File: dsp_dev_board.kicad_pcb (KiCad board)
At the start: 4 copper layers, 100 x 72.6 mm, 92 parts, among them J1 aux_mcu_power, J10 DX07S016JA1R1500, J11 Conn_02x11_Odd_Even, J2 audio_in, J3 audio_out, J4 9v_jack, J5 input_jack, J6 output_jack, J7 digital, J8 analog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

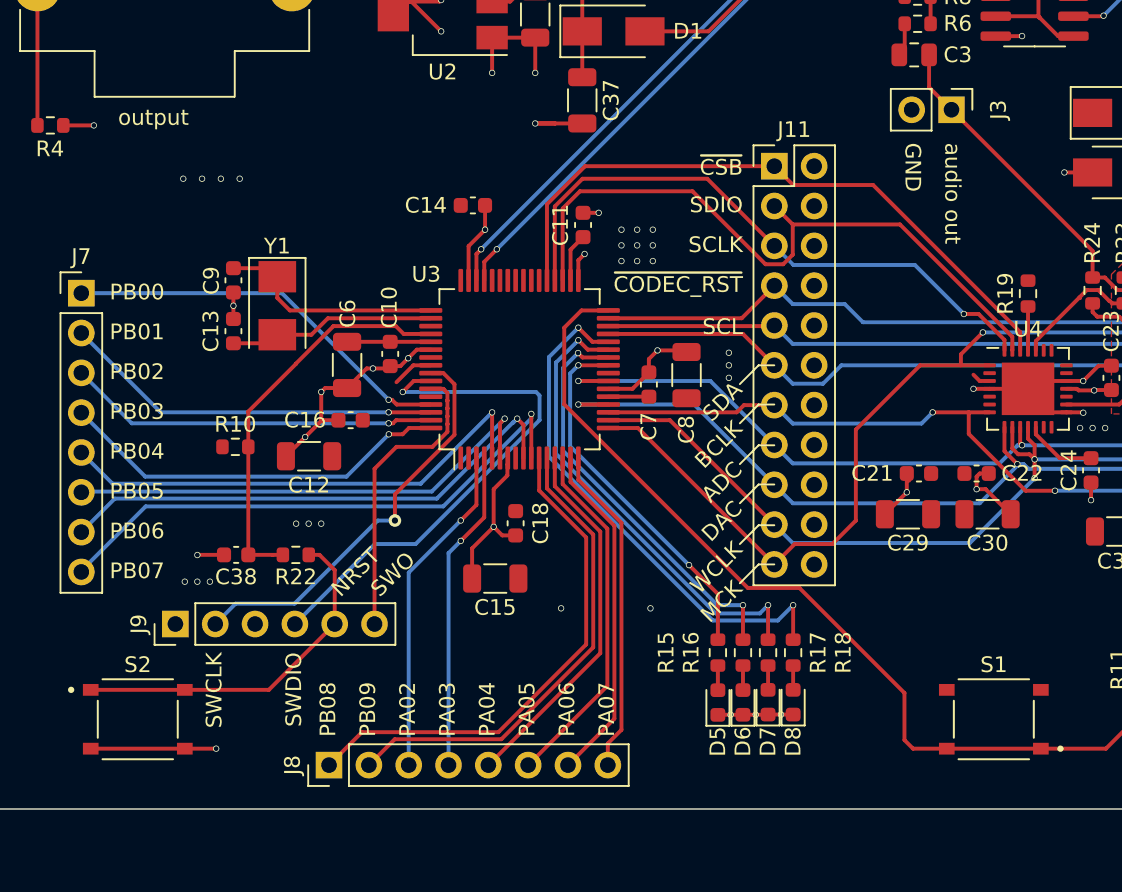
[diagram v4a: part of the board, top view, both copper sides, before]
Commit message: add boot/reset labels for the switches
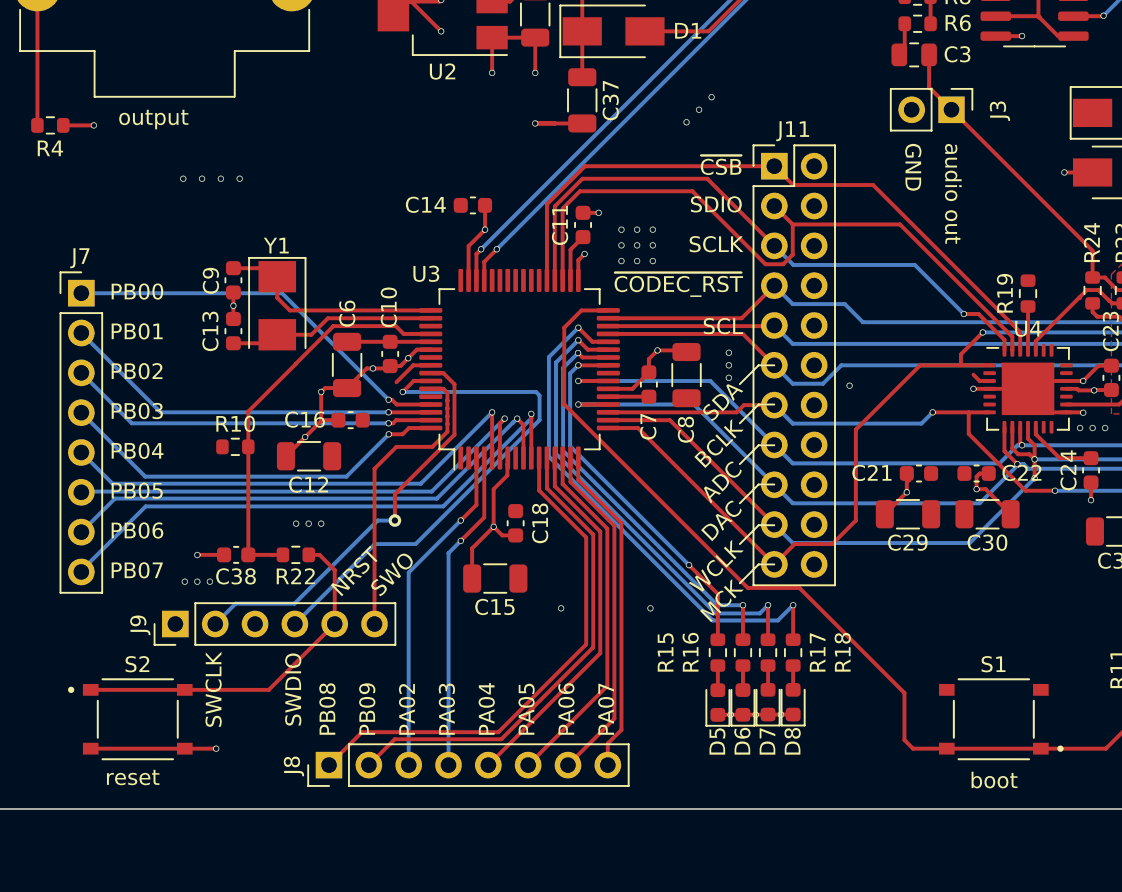
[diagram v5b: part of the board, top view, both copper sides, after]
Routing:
- net 3.3V: vias 36 -> 40
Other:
- board text added: "boot"
- board text added: "reset"
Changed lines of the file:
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@@
   (general
     (thickness 1.6)
-    (drawings 57)
-    (tracks 814)
+    (drawings 59)
+    (tracks 818)
     (zones 0)
     (modules 92)
@@
            (xy -0.210436 0.321292)) (width 0.163642))
       ))
-    (pad "" smd roundrect (at 0.5 0.5) (size 0.806226 0.806226) (layers F.Paste) (roundrect_rratio 0.25))
-    (pad "" smd roundrect (at 0.5 -0.5) (size 0.806226 0.806226) (layers F.Paste) (roundrect_rratio 0.25))
-    (pad "" smd roundrect (at -0.5 0.5) (size 0.806226 0.806226) (layers F.Paste) (roundrect_rratio 0.25))
-    (pad "" smd roundrect (at -0.5 -0.5) (size 0.806226 0.806226) (layers F.Paste) (roundrect_rratio 0.25))
+    (pad "" smd roundrect (at 0.5 0.5) (size 0.806226 0.806226) (layers F.Paste) (roundrect_rratio 0.2499993798265003))
+    (pad "" smd roundrect (at 0.5 -0.5) (size 0.806226 0.806226) (layers F.Paste) (roundrect_rratio 0.2499993798265003))
+    (pad "" smd roundrect (at -0.5 0.5) (size 0.806226 0.806226) (layers F.Paste) (roundrect_rratio 0.2499993798265003))
+    (pad "" smd roundrect (at -0.5 -0.5) (size 0.806226 0.806226) (layers F.Paste) (roundrect_rratio 0.2499993798265003))
     (pad 33 smd rect (at 0 0) (size 2.5 2.5) (layers B.Cu)
       (net 1 GND))
@@
     )
   )
+  (gr_text reset (at 99.0625 110.6) (layer F.SilkS)
+    (effects (font (size 1 1) (thickness 0.15)))
+  )
+  (gr_text boot (at 154 110.8) (layer F.SilkS)
+    (effects (font (size 1 1) (thickness 0.15)))
+  )
   (gr_text "ARM Effects v1\nfor WM8731\nand TLV320AIC3105, 3109\n\n© 2021\nEric Wood, Matt Mullins" (at 176.6 104) (layer F.SilkS)
     (effects (font (size 1 1) (thickness 0.15)))
@@
   (segment (start 178.35 81.55) (end 178.35 83.4625) (width 0.25) (layer F.Cu) (net 2))
   (segment (start 178.45 81.45) (end 178.35 81.55) (width 0.25) (layer F.Cu) (net 2))
+  (via (at 134.4 68.8) (size 0.4) (drill 0.3) (layers F.Cu B.Cu) (net 2))
+  (via (at 135.2 68) (size 0.4) (drill 0.3) (layers F.Cu B.Cu) (net 2))
+  (via (at 136 67.2) (size 0.4) (drill 0.3) (layers F.Cu B.Cu) (net 2))
+  (via (at 144.8 85.6) (size 0.4) (drill 0.3) (layers F.Cu B.Cu) (net 2))
   (segment (start 167.574999 57.1) (end 170.7 60.225001) (width 0.25) (layer F.Cu) (net 3) (status 20))
   (segment (start 165.03 57.1) (end 167.574999 57.1) (width 0.25) (layer F.Cu) (net 3) (status 10))
